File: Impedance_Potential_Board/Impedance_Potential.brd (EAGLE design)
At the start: 70 x 70 mm, 39 parts, among them IC1 MAX30001GCWV+, U4 AP2112K-1.8V

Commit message: MAX30001G
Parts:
- removed SJ4: LED DISABLE, SparkFun-Jumpers:SMT-JUMPER_2_NC_TRACE_NO-SILK
- added AOUT, BIN, BIP, DRVN, DRVP, ECGN, ECGP: TEST-POINT3, SparkFun-Connectors:PAD.03X.03
- added BP_BN, DN_BN, DP_BP, EC_UNBAL, EN_BN, EN_UNBAL, EP_BP, EP_EN, EP_UNBAL, RBN, RBP: JUMPER-SMT_2_NO_SILK, SparkFun-Jumpers:SMT-JUMPER_2_NO_SILK
- added C21: 10uF, SparkFun-Capacitors:0603
- added C22, C23, C24: 47nF, SparkFun-Capacitors:0603
- added D2, D3, D4, D5, D6, D7, D8: ESD7551N2T5G, ESD7551N2T5G:ESD7551N2T5G
- added ECGC: ECGC, SparkFun-Connectors:PAD.03X.03
- added FCLK: FCLK, SparkFun-Connectors:PAD.03X.03
- added J1: (no value), SparkFun-Connectors:1X08
- added LED_ENABLE: LED ENABLE, SparkFun-Jumpers:SMT-JUMPER_2_NC_PASTE_SILK
- added P_DWN_ENABLE, P_UP_ENABLE: JUMPER-SMT_2_NC_PASTE_SILK, SparkFun-Jumpers:SMT-JUMPER_2_NC_PASTE_SILK
- added R11, R12, R13, R14, R15, R17: 100k, SparkFun-Resistors:0603
- added R18: 100, SparkFun-Resistors:0603
- C1, C2: value 47nF -> 0.22uF
- C11, C12, C13, C14, C17, C19, C20: device rcl:C0603 -> SparkFun-Capacitors:0603
- R1, R2, R3: value 200k -> 47k
- R10, R5, R6, R7, R8, R9: value 10M -> 10
- moved R10 231.2 mm to (37.0, 57.0), turned to 270 degrees
- moved R9 228.4 mm to (39.5, 57.0), turned to 270 degrees
- moved R8 225.6 mm to (42.1, 57.0), turned to 270 degrees
- moved R7 222.8 mm to (44.6, 57.0), turned to 270 degrees
- moved R6 220.2 mm to (47.2, 57.0), turned to 270 degrees
- moved R5 217.5 mm to (49.7, 57.0), turned to 270 degrees
- moved C20 214.5 mm to (40.5, 34.5)
- moved C19 195.7 mm to (40.5, 41.5), turned to 180 degrees
- moved C18 185.2 mm to (29.5, 41.5)
- moved C14 172.8 mm to (29.5, 48.8), turned to 180 degrees
- moved C17 172.6 mm to (29.5, 43.5), turned to 180 degrees
- moved C13 166.5 mm to (29.5, 47.2), turned to 180 degrees
- moved C12 162.4 mm to (39.0, 45.0)
- moved C16 157.1 mm to (41.8, 49.2), turned to 270 degrees
- moved C11 156.3 mm to (39.0, 43.5)
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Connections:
- net N$10 renamed CAPP
- net N$11 renamed CAPN
- net N$12 renamed VREF
- net N$16 renamed VBG
- net N$17 renamed RBIAS
- net N$18 renamed CSB_
- net N$2 renamed DRVP_
- net N$20 renamed CPLL
- net N$21 renamed SCLK_
- net N$22 renamed SDI_
- net N$23 renamed SDO_
- net N$24 renamed INT2B_
- net N$25 renamed INTB_
- net N$4 renamed DRVN_
- removed net N$1: C1.2, DRV.2
- removed net N$13: C3.1, C5.1, IC1.A3, IMPEDANCE.3
- removed net N$14: ECG.3, R2.2
- removed net N$15: C7.2, C8.2, IC1.A6, R2.1
- removed net N$19: C11.1, C12.1, C15.2, C17.1, IC1.D6, IC1.E1, U4.5
- removed net N$27: IC1.D5
- removed net N$3: ECG.2, R1.2
- removed net N$5: C2.2, DRV.3
- removed net N$6: C4.2, C5.2, IC1.A4, IMPEDANCE.2
- removed net N$7: ECG.1, R3.2
- removed net N$8: C20.1, IC1.C1, R3.1
- removed net N$9: C6.1, C8.1, IC1.A5, R1.1
- removed net VDD: C13.1, C14.1, C16.2, IC1.D3, U4.1, U4.3
- new net 1.8V: C11.1, C12.1, C15.2, C17.1, C21.1, IC1.D6, IC1.E1, U4.5
- new net AOUT: AOUT.P$1, IC1.C2
- new net BIN: BIN.P$1, BP_BN.2, C3.1, C5.1, D4.1, DN_BN.1, EN_BN.2, IC1.A3, IMPEDANCE.3, RBN.2
- new net BIP: BIP.P$1, BP_BN.1, C4.2, C5.2, D5.1, DP_BP.1, EP_BP.2, IC1.A4, IMPEDANCE.2, RBP.1
- new net CSB: J1.1, R10.1, R15.2
- new net DRVN: C2.2, D3.1, DN_BN.2, DRV.3, DRVN.P$1
- new net DRVP: C1.2, D2.1, DP_BP.2, DRV.2, DRVP.P$1
- new net ECGC: C24.2, D6.2, ECG.1, ECGC.P$1, EC_UNBAL.1, R3.2
- new net ECGN: C23.2, D8.2, ECG.3, ECGN.P$1, EN_BN.1, EN_UNBAL.1, R2.2
- new net ECGN_: C23.1, C7.2, C8.2, EN_UNBAL.2, EP_EN.1, IC1.A6, R2.1
- new net ECGP: C22.2, D7.2, ECG.2, ECGP.P$1, EP_BP.1, EP_UNBAL.1, R1.2
- new net ECGP_: C22.1, C6.1, C8.1, EP_EN.2, EP_UNBAL.2, IC1.A5, R1.1
- new net FCLK_: FCLK.P$1, IC1.D5
- new net INT1B: J1.6, R14.2, R5.1
- new net INT2B: J1.5, R17.2, R6.1
- new net N$29: P_DWN_ENABLE.2, R11.1, R12.1, R13.1
- new net N$30: P_UP_ENABLE.2, R14.1, R15.1, R17.1
- new net N$32: R18.2, RBN.1
- new net N$33: R18.1, RBP.2
- new net SCLK: J1.2, R13.2, R9.1
- new net SDI: J1.3, R11.2, R8.1
- new net SDO: J1.4, R12.2, R7.1
- new net VCM: C20.1, C24.1, EC_UNBAL.2, IC1.C1, R3.1
- net 3.3V: now also C13.1, C14.1, C16.2, IC1.D3, J1.7, P_UP_ENABLE.1, U4.1, U4.3
- net GND: now also C21.2, D2.2, D3.2, D4.2, D5.2, D6.1, D7.1, D8.1, J1.8, LED_ENABLE.1, P_DWN_ENABLE.1; no longer SJ4.1
- net N$28: now also LED_ENABLE.2; no longer SJ4.2
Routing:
- net 3.3V: track 0.00 -> 121.2 mm, vias 0 -> 2
- net BIN: track 0.00 -> 56.4 mm, vias 0 -> 2
- net BIP: track 0.00 -> 52.7 mm
- net ECGN: track 0.00 -> 45.0 mm
- net ECGC: track 0.00 -> 38.4 mm, vias 0 -> 2
- net DRVN: track 0.00 -> 34.4 mm
- net DRVP: track 0.00 -> 30.4 mm, vias 0 -> 2
- net ECGP: track 0.00 -> 28.1 mm
- net ECGN_: track 0.00 -> 26.1 mm
- net DRVP_: track 0.00 -> 25.3 mm
- net N$30: track 0.00 -> 23.5 mm, vias 0 -> 4
- net 1.8V: track 0.00 -> 23.0 mm
- net INTB_: track 0.00 -> 22.2 mm, vias 0 -> 2
- net VCM: track 0.00 -> 20.9 mm, vias 0 -> 2
- net DRVN_: track 0.00 -> 20.7 mm
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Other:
- board text added: "MAX30001G Board MediBrick2000"
- board text removed: "AD5933 Bioimpedance Board MediBrick2000"

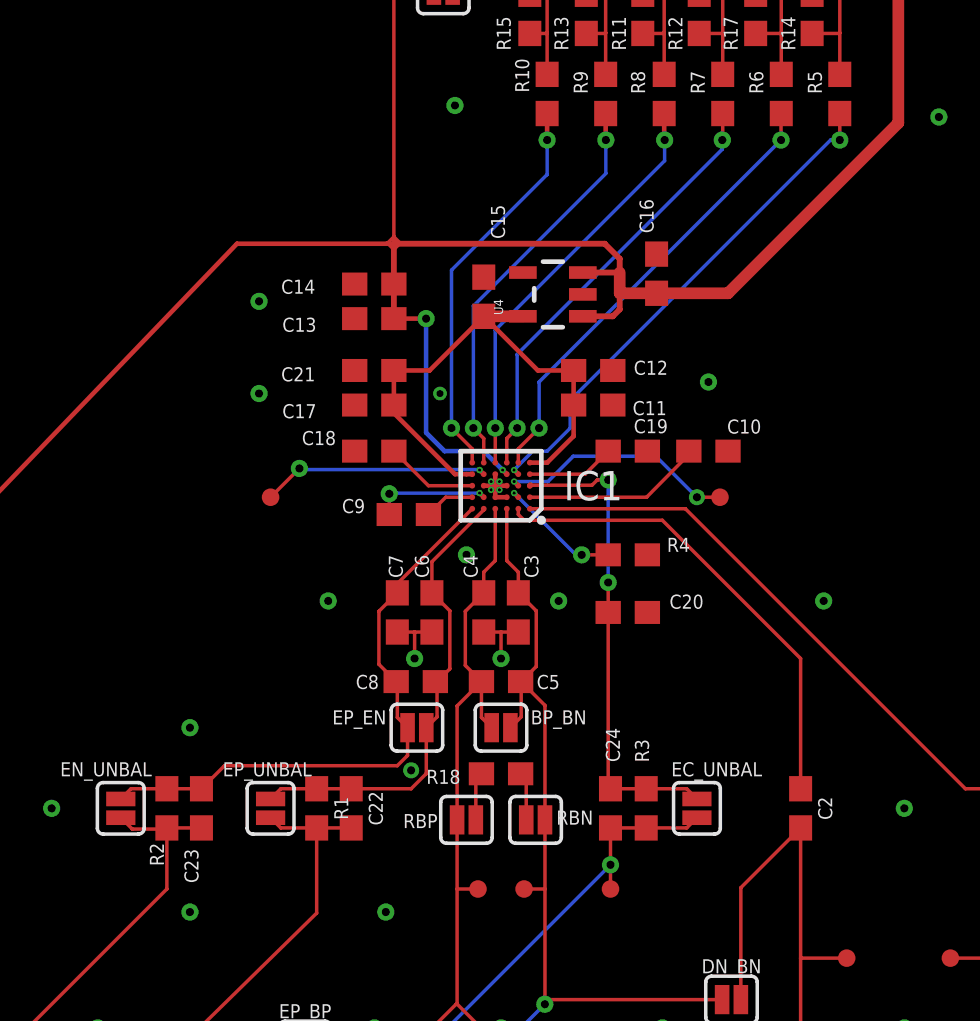
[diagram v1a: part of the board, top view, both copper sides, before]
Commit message: BOM MAX30001G and board updates
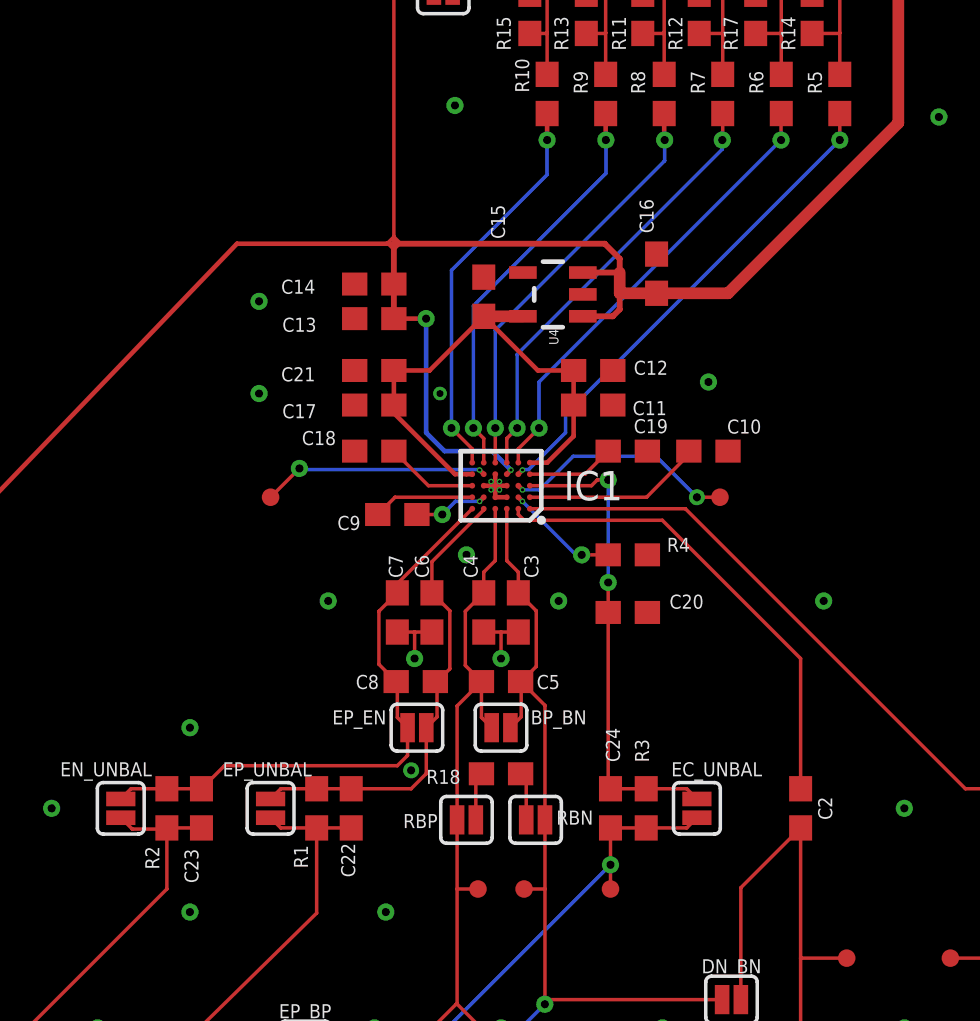
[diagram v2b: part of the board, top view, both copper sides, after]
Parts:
- C9: value 1.0uF -> 10uF
- R1, R2, R3: value 47k -> 51k
- R4: value 330k -> 324k
- moved C9 0.50 mm to (30.5, 38.8), turned to 180 degrees
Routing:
- net CAPP: track 2.21 -> 4.41 mm
- net CAPN: track 5.09 -> 3.21 mm
- net INTB_: track 22.2 -> 21.6 mm
- net RBIAS: track 5.44 -> 4.94 mm

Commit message: CAM Impedance_Potential Board
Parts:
- added R19, R20, R21, R22, R23: 0, SparkFun-Resistors:0603
- J1: value (none) -> Header
- moved EC_UNBAL 18.2 mm to (26.0, 21.0)
- moved R3 14.2 mm to (28.0, 21.0)
- moved ECGC 11.4 mm to (29.2, 18.0)
- moved C24 11.4 mm to (29.5, 21.0)
- moved EN_BN 10.4 mm to (19.0, 15.8), flipped to the bottom, turned to 180 degrees
- moved C23 8.30 mm to (15.3, 21.1)
- moved EN_UNBAL 8.30 mm to (11.8, 21.1)
- moved R2 8.30 mm to (13.8, 21.1)
- moved C22 7.81 mm to (22.5, 21.0)
- moved EP_UNBAL 7.81 mm to (19.0, 21.0)
- moved R1 7.81 mm to (21.0, 21.0)
- moved BIN 4.50 mm to (36.0, 18.0)
- moved BIP 4.50 mm to (34.0, 18.0)
- moved R18 4.50 mm to (35.0, 23.0)
- moved RBN 4.50 mm to (36.5, 21.0)
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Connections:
- new net N$1: C23.1, EN_UNBAL.2, R2.1, R22.2
- new net N$2: C24.1, EC_UNBAL.2, R23.2, R3.1
- new net N$3: C22.1, EP_UNBAL.2, R1.1, R21.2
- new net N$4: BP_BN.2, C3.1, C5.1, IC1.A3, R19.1
- new net N$5: BP_BN.1, C4.2, C5.2, IC1.A4, R20.1
- net BIN: now also R19.2; no longer BP_BN.2, C3.1, C5.1, IC1.A3
- net BIP: now also R20.2; no longer BP_BN.1, C4.2, C5.2, IC1.A4
- net ECGN_: now also R22.1; no longer C23.1, EN_UNBAL.2, R2.1
- net ECGP_: now also R21.1; no longer C22.1, EP_UNBAL.2, R1.1
- net VCM: now also R23.1; no longer C24.1, EC_UNBAL.2, R3.1
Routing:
- net N$1: track 0.00 -> 20.2 mm
- net N$2: track 0.00 -> 18.5 mm, vias 0 -> 2
- net BIP: track 52.7 -> 35.8 mm, vias 0 -> 2
- net ECGN: track 45.0 -> 28.7 mm, vias 0 -> 1
- net N$3: track 0.00 -> 14.7 mm
- net N$4: track 0.00 -> 12.8 mm
- net N$5: track 0.00 -> 12.8 mm
- net ECGN_: track 26.1 -> 14.2 mm
- net ECGC: track 38.4 -> 28.5 mm, vias 2 -> 0
- net ECGP: track 28.1 -> 20.4 mm, vias 0 -> 1
- net BIN: track 56.4 -> 49.2 mm, vias 2 -> 3
- net ECGP_: track 20.5 -> 13.8 mm
- net GND: track 8.92 -> 15.0 mm, vias 38 -> 37
- net DRVN: track 34.4 -> 28.7 mm, vias 0 -> 1
- net VCM: track 20.9 -> 16.4 mm
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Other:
- board text added: "3.3V"
- board text added: "CSB"
- board text added: "GND"
- board text added: "INT1B"
- board text added: "INT2B"
- board text added: "SCLK"
- board text added: "SDI"
- board text added: "SDO"

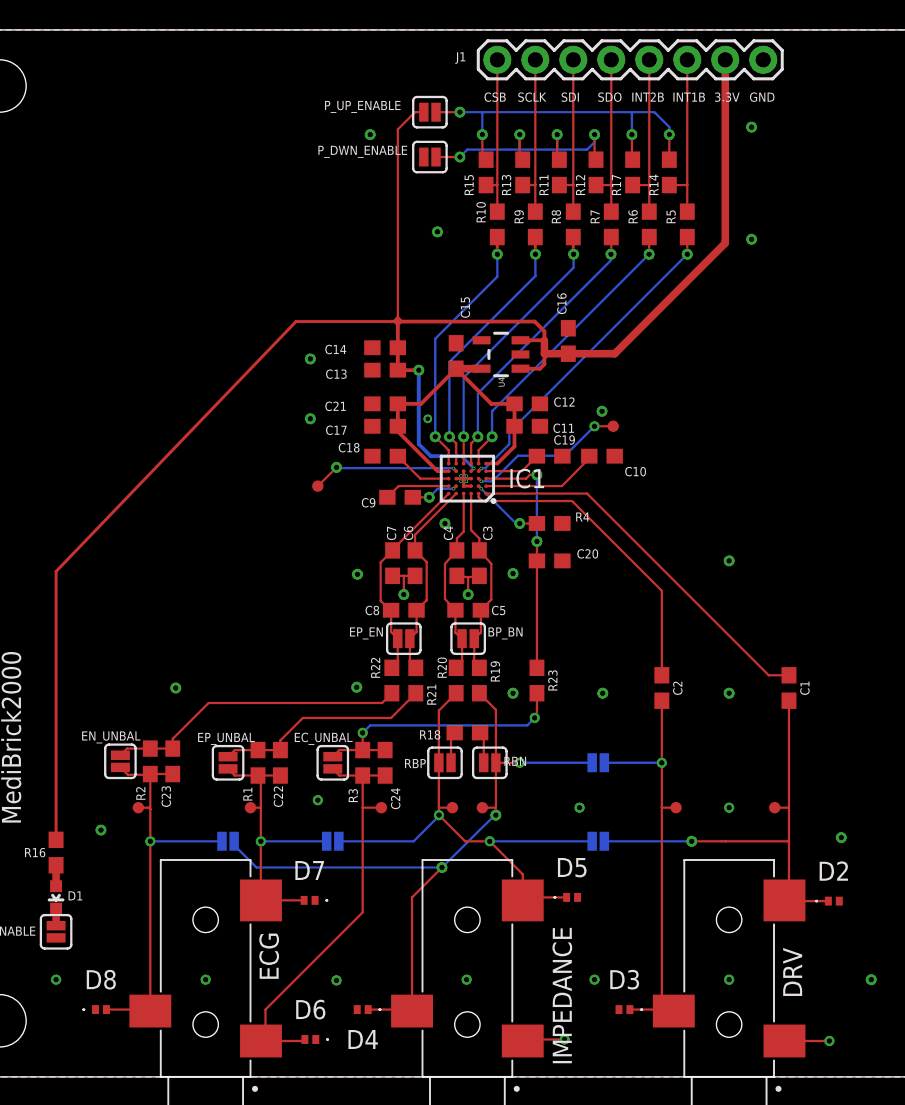
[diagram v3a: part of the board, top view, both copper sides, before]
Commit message: 3 Channel Analog Temp
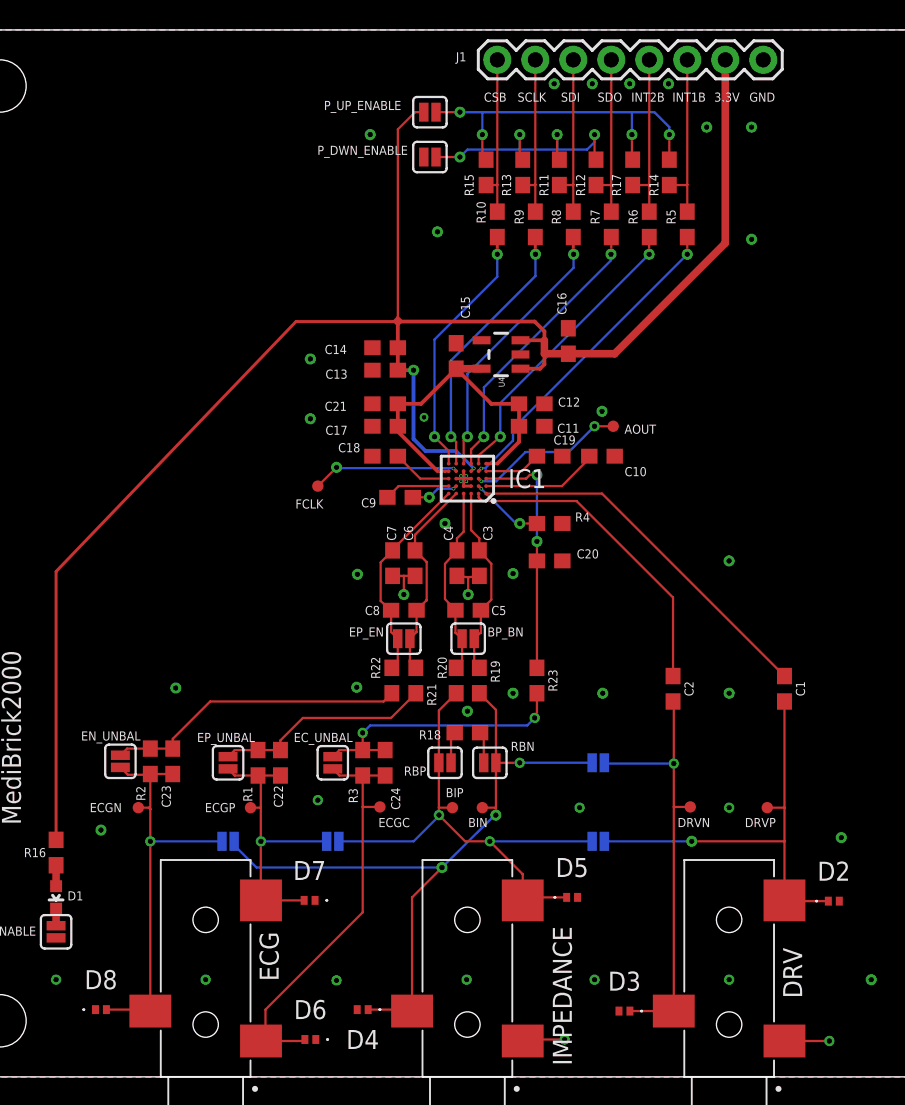
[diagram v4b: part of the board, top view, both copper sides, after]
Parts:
- moved DRVN 0.95 mm to (49.9, 18.1)
- moved C2 0.75 mm to (48.8, 25.9)
- moved DRVP 0.50 mm to (55.0, 18.0)
- moved C1 0.30 mm to (56.2, 25.9)
- moved C11 0.30 mm to (39.3, 43.5)
- moved C12 0.30 mm to (39.3, 45.0)
- moved ECGC 0.11 mm to (29.1, 18.1)
- moved D3 0.10 mm to (45.5, 4.40)
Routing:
- net DRVN: track 28.7 -> 29.4 mm
- net DRVN_: track 20.7 -> 21.3 mm
- net ECGN: track 28.7 -> 28.2 mm
- net GND: vias 37 -> 43
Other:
- board text added: "AOUT"
- board text added: "BIN"
- board text added: "BIP"
- board text added: "DRVN"
- board text added: "DRVP"
- board text added: "ECGC"
- board text added: "ECGN"
- board text added: "ECGP"
- board text added: "FCLK"

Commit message: Cleanup, organization and updates
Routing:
- net N$29: track 18.7 -> 16.4 mm
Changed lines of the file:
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@@
 <drawing>
 <settings>
-<setting alwaysvectorfont="yes"/>
+<setting alwaysvectorfont="no"/>
 <setting verticaltext="up"/>
 </settings>
@@
 <wire x1="43.6" y1="61.325" x2="43.5" y2="61.425" width="0.1524" layer="1"/>
 <wire x1="43.5" y1="61.425" x2="43.5" y2="63" width="0.1524" layer="1"/>
-<wire x1="34.5" y1="61.5" x2="35" y2="62" width="0.1524" layer="16"/>
-<wire x1="35" y1="62" x2="38.5" y2="62" width="0.1524" layer="16"/>
-<wire x1="38.5" y1="62" x2="41" y2="62" width="0.1524" layer="16"/>
-<wire x1="41" y1="62" x2="43" y2="62" width="0.1524" layer="16"/>
-<wire x1="43.5" y1="63" x2="43.5" y2="62.5" width="0.1524" layer="16"/>
-<wire x1="43.5" y1="62.5" x2="43" y2="62" width="0.1524" layer="16"/>
-<wire x1="41" y1="63" x2="41" y2="62" width="0.1524" layer="16"/>
-<wire x1="38.5" y1="63" x2="38.5" y2="62" width="0.1524" layer="16"/>
+<wire x1="38.5" y1="63" x2="37" y2="61.5" width="0.1524" layer="16"/>
+<wire x1="34.5" y1="61.5" x2="37" y2="61.5" width="0.1524" layer="16"/>
+<wire x1="38.5" y1="63" x2="41" y2="63" width="0.1524" layer="16"/>
+<wire x1="41" y1="63" x2="43.5" y2="63" width="0.1524" layer="16"/>
 </signal>
 <signal name="N$30">

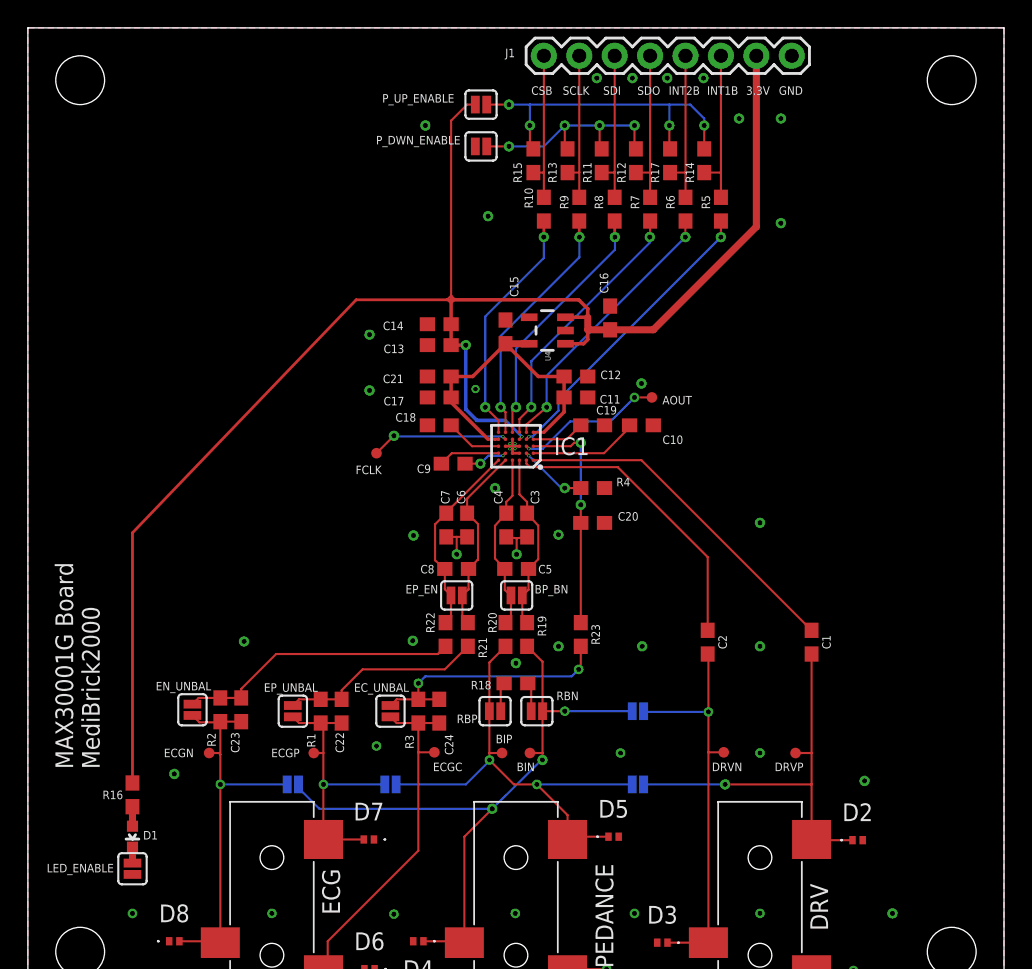
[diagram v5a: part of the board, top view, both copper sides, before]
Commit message: Board Updates
All LEDs at same location
Separated analog and digital ground
Updated impedance components
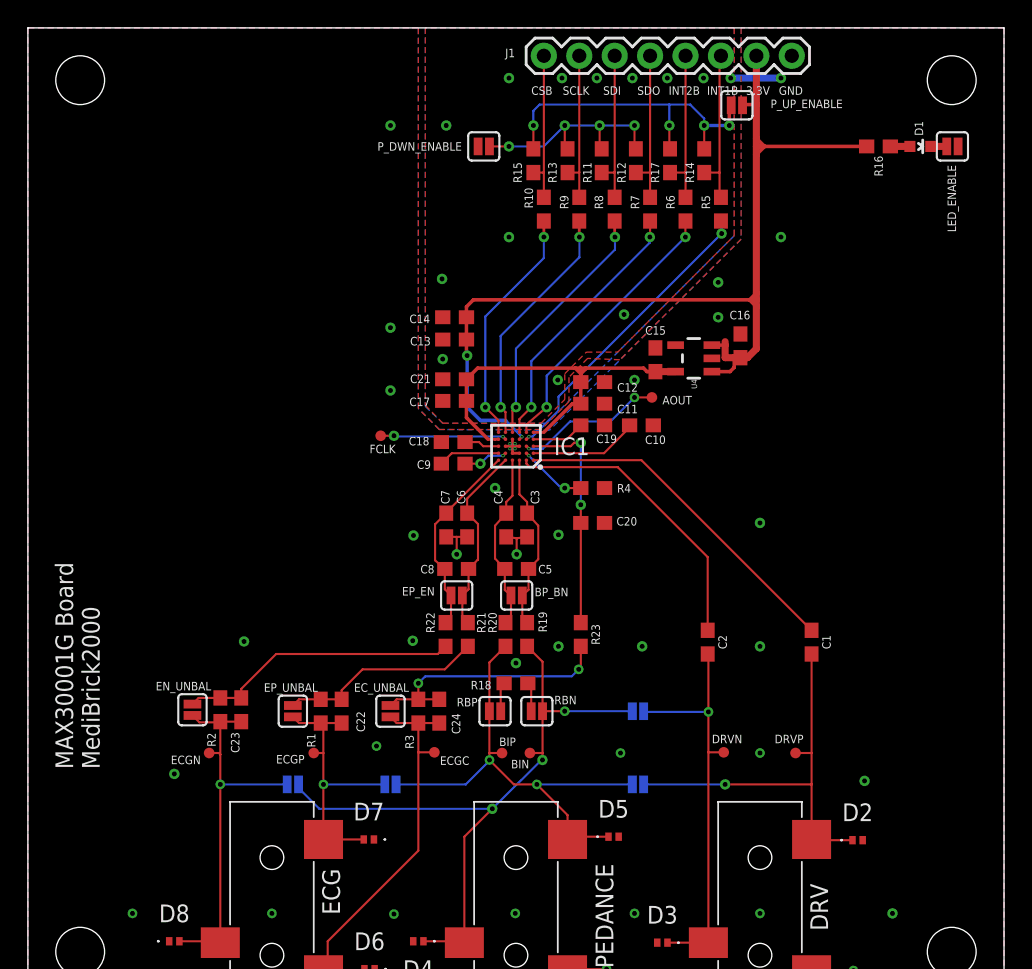
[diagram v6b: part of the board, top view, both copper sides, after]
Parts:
- moved LED_ENABLE 78.4 mm to (66.3, 61.5), turned to 180 degrees
- moved D1 75.1 mm to (64.0, 61.5), turned to 270 degrees
- moved R16 70.9 mm to (61.0, 61.5), turned to 180 degrees
- moved P_UP_ENABLE 18.4 mm to (50.8, 64.5), turned to 180 degrees
- moved C15 10.9 mm to (45.0, 46.2)
- moved U4 10.7 mm to (47.8, 46.3)
- moved C16 9.56 mm to (51.1, 47.2)
- moved C18 1.56 mm to (30.5, 40.3)
- moved FCLK 1.29 mm to (25.3, 40.8)
- moved C11 1.28 mm to (40.5, 43.0)
- moved C12 1.26 mm to (40.5, 44.6)
- moved C14 1.21 mm to (30.6, 49.2)
- moved C13 1.17 mm to (30.6, 47.6)
- moved C17 1.13 mm to (30.6, 43.2)
- moved C21 1.12 mm to (30.6, 44.8)
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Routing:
- net 3.3V: track 121.5 -> 73.3 mm
- net 1.8V: track 23.4 -> 29.0 mm
- net GND: track 15.0 -> 18.6 mm, vias 43 -> 51
- net CPLL: track 4.02 -> 2.52 mm
- net FCLK_: track 9.87 -> 9.05 mm
